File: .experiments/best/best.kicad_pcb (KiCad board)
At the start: 2 copper layers, 140 x 90 mm, 39 parts, among them J1 USB_C, J2 Output, J3 Debug, Q1 FS8205A, U1 USBLC6-2SC6, U2 BQ24072, U3 HY2113-KB5B, U4 MT3608, U5 AP2112K-3.3, U6 LN61CN3302MR-G

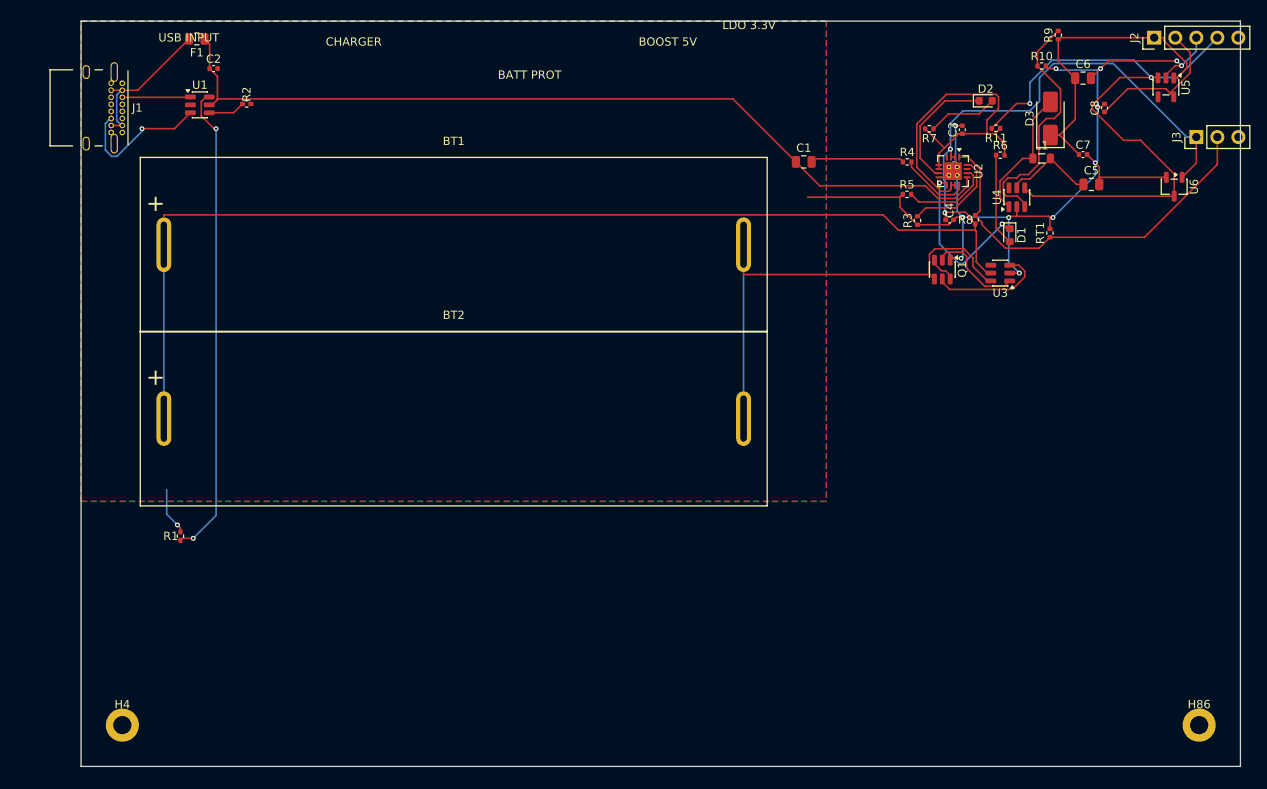
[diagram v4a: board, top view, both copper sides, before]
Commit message: Fix placement, start/stop lifecycle, frame gen, battery overlap, and silkscreen labels
Placement fixes:
- Randomize edge component positions instead of deterministic pinning
- Fix _clamp_pads_to_board bug (separate shift tracking + max_y typo)
- Add THT detection and backside layer assignment for large through-hole parts
- Enable board size search with 70/30 shrink bias
- Increase area weight from 5% to 10%

Start/stop lifecycle:
- FreeRouting subprocess uses process groups (start_new_session + killpg)
- ExperimentRunner uses process groups for clean termination
- SIGTERM handler in autoexperiment creates stop.now for graceful shutdown
- Write 'stopping' phase to status JSON, cancel futures mid-batch
- Singleton ExperimentRunner on AppState (no lost Popen references)
- GUI button state machine: Start/Stop/Force Kill with stopping spinner

Frame generation:
- Log warnings instead of silently swallowing snapshot_pcb errors
- Pre-flight check for kicad-cli and magick availability
- Remove dead round_num_local variable

Battery courtyard overlap:
- Split BT1/BT2 zones to bottom-left/bottom-right
- Resolve locked-locked overlaps by moving smaller component
- 15pt penalty for large component overlaps (vs 5pt normal)

Silkscreen group labels:
- Regenerate group labels on final output PCB via add_group_labels()
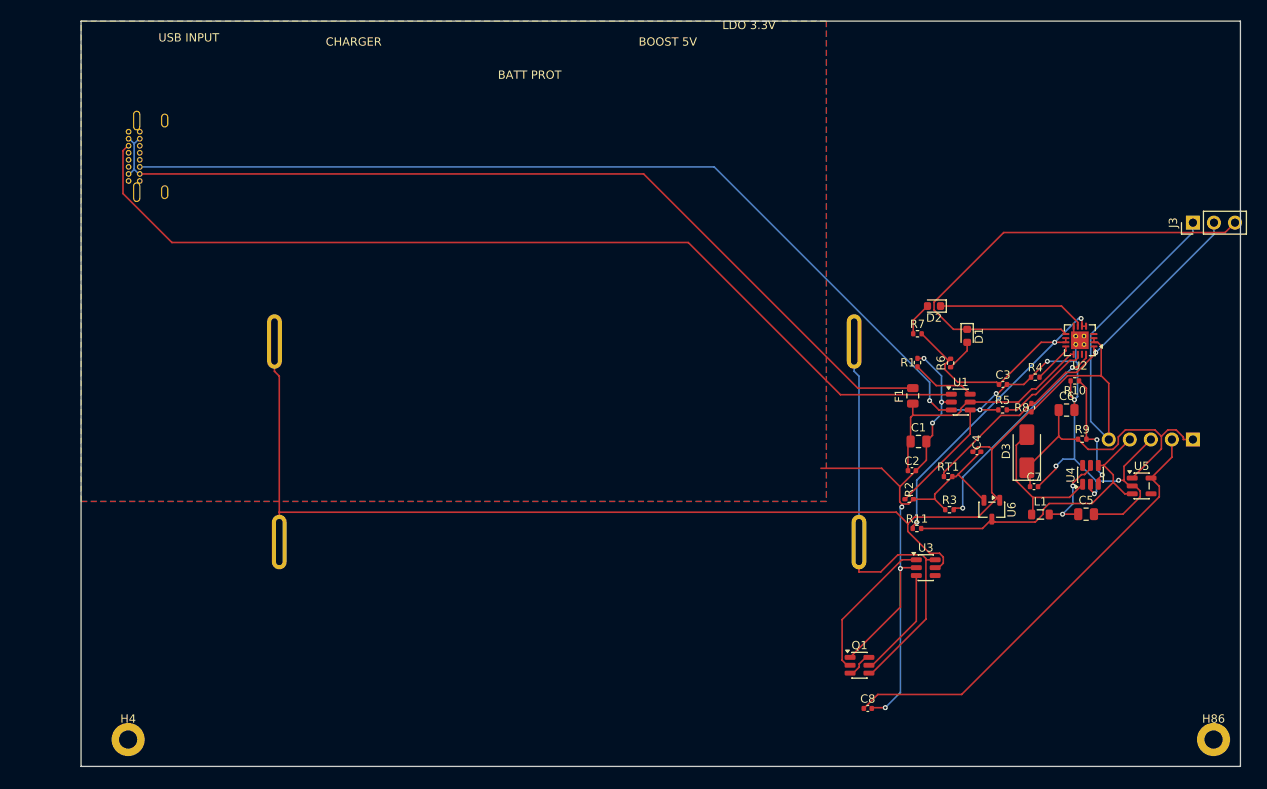
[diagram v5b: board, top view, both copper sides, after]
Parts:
- BT1, BT2, J1, J2: moved to B.Cu
- moved U1 98.6 mm to (106.2, 46.0)
- moved C2 97.3 mm to (100.3, 54.3)
- moved F1 96.6 mm to (100.4, 45.3), turned to 90 degrees
- moved R2 93.2 mm to (100.0, 57.7)
- moved R1 91.4 mm to (101.0, 41.2)
- moved C8 77.9 mm to (95.0, 83.0), turned to 0 degrees
- moved R11 49.3 mm to (100.9, 61.3), turned to 0 degrees
- moved R9 48.9 mm to (120.9, 50.5), turned to 0 degrees
- moved Q1 48.8 mm to (94.0, 77.8), turned to 0 degrees
- moved J2 48.7 mm to (134.3, 50.5)
- moved U5 48.2 mm to (128.1, 56.1), turned to 0 degrees
- moved U6 44.8 mm to (110.0, 59.0)
- moved L1 43.0 mm to (115.8, 59.6)
- moved C7 40.5 mm to (115.1, 56.2)
- moved D3 40.3 mm to (114.2, 51.9)
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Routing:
- net Net-(J1-CC1): track 8.23 -> 116.2 mm
- net Net-(J1-CC2): track 17.1 -> 111.5 mm
- net Net-(F1-Pad2): track 18.2 -> 110.8 mm
- net /VBUS: track 106.4 -> 31.0 mm
- net Net-(R1-Pad1): track 57.6 -> 7.73 mm, vias 2 -> 0
- net /EN: track 79.1 -> 36.6 mm, vias 2 -> 0
- net /CHG_N: track 20.1 -> 58.4 mm, vias 2 -> 0
- net /3V3: track 18.4 -> 54.6 mm
- net GND: track 142.2 -> 169.6 mm
- net Net-(U4-FB): track 29.9 -> 14.5 mm, vias 0 -> 2
- net /VSYS: track 45.0 -> 59.6 mm, vias 0 -> 3
- net Net-(U2-ISET): track 12.0 -> 26.2 mm, vias 0 -> 2
- net Net-(R2-Pad1): track 4.45 -> 14.0 mm
- net Net-(D1-A): track 11.1 -> 3.83 mm
- net Net-(Q1A-G): track 11.6 -> 18.1 mm
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
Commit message: Fix 10 experiment issues: zones, DRC, edge compliance, gates, retry
- Strip pre-existing F.Cu/B.Cu zones via subprocess before routing
- Patch DSN smd_smd clearance from 0.05mm to match KiCad 0.2mm rule
- Fix edge_compliance scoring margin (3mm -> edge_margin + 2.0)
- Lower placement gates: min_placement 30->20, courtyard 50->10
- Add FreeRouting retry on crash (2 attempts, reduced passes)
- Zone refill after routing, before DRC
- ensure_gnd_zone runs in subprocess (avoids SWIG corruption)
- Elite archive stale min_placement_score override
- SWIG output parsing fix for strip_zones

Results: score 90.25->92.17, DRC 114->45 (-60%), 0 crashes
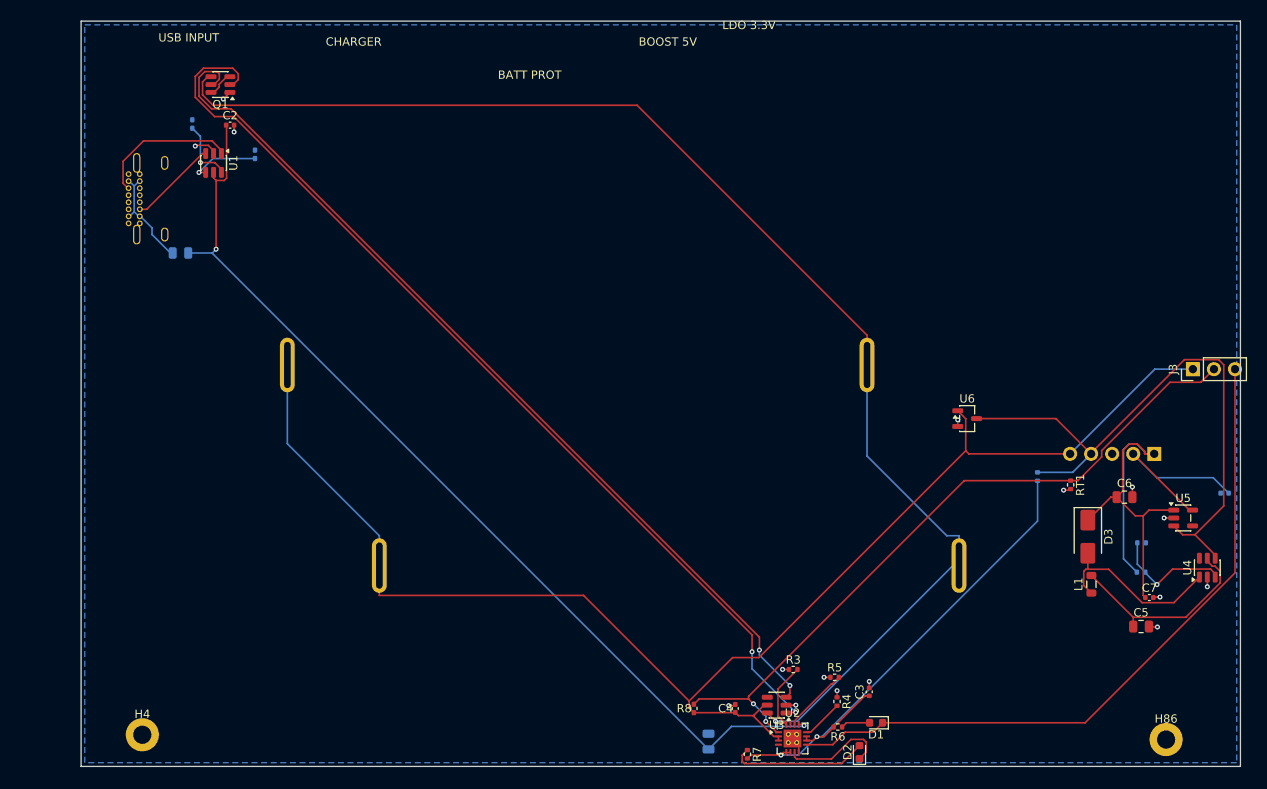
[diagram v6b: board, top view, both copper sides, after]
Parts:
- C1, C8, F1, R1, R10, R11, R2, R9: moved to B.Cu
- moved Q1 104.3 mm to (16.8, 7.66), turned to 180 degrees
- moved U1 94.7 mm to (16.0, 17.1), turned to -90 degrees
- moved C2 92.3 mm to (18.0, 12.6)
- moved R1 92.2 mm to (13.4, 12.4)
- moved F1 90.1 mm to (12.0, 28.0), turned to 180 degrees
- moved R2 89.3 mm to (21.0, 16.1), turned to 90 degrees
- moved U2 59.3 mm to (85.9, 86.6), turned to 0 degrees
- moved R7 54.8 mm to (80.5, 88.5), turned to -90 degrees
- moved D2 54.6 mm to (94.0, 88.3), turned to 90 degrees
- moved R8 54.6 mm to (74.0, 83.0)
- moved C8 50.3 mm to (138.1, 57.0), turned to 180 degrees
- moved D1 48.0 mm to (96.0, 84.7), turned to 180 degrees
- moved R6 46.0 mm to (91.4, 85.2), turned to 180 degrees
- moved R4 45.9 mm to (91.3, 82.2), turned to -90 degrees
- moved C1 44.2 mm to (75.8, 87.0), turned to 90 degrees
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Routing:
- net GND: track 169.6 -> 19.1 mm, vias 13 -> 16
- net /CELL_NEG: track 55.2 -> 160.1 mm, vias 0 -> 1
- net Net-(J1-CC2): track 111.5 -> 10.7 mm, vias 1 -> 0
- net Net-(Q1A-G): track 18.1 -> 117.2 mm, vias 0 -> 2
- net Net-(J1-CC1): track 116.2 -> 17.3 mm
- net Net-(F1-Pad2): track 110.8 -> 13.0 mm
- net Net-(Q1B-G): track 13.4 -> 110.8 mm, vias 0 -> 2
- net /VBUS: track 31.0 -> 119.0 mm, vias 0 -> 2
- net /NTC_SENSE: track 47.4 -> 85.8 mm, vias 1 -> 2
- net /EN: track 36.6 -> 72.9 mm
- net /3V3: track 54.6 -> 23.5 mm
- net /CHG_N: track 58.4 -> 84.9 mm
- net /VBAT: track 193.0 -> 173.9 mm
- net Net-(U2-ISET): track 26.2 -> 8.03 mm, vias 2 -> 0
- net /5V: track 37.1 -> 53.6 mm
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- removed copper zone on F.Cu, net GND
